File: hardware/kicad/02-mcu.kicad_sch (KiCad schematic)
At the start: 7 parts, among them U1 ESP32-S3-N16R8

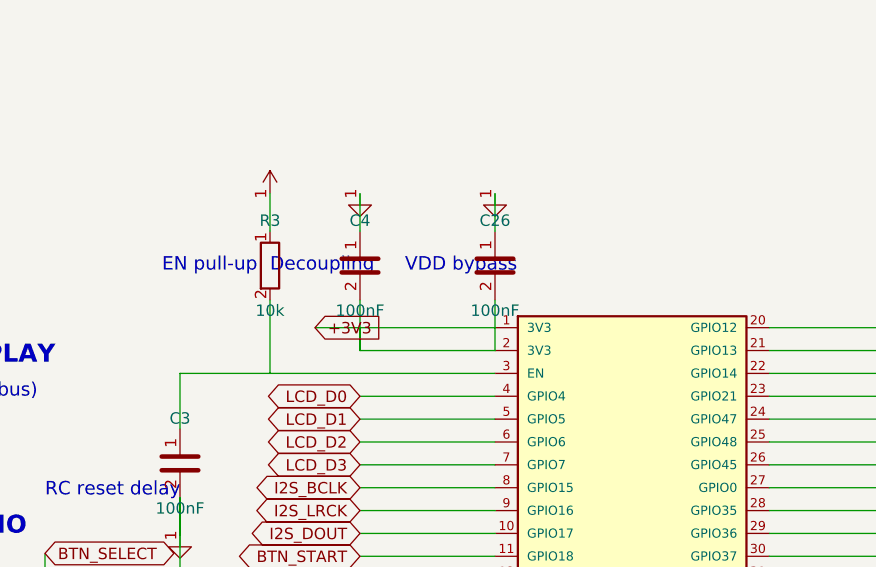
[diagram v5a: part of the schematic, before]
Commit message: fix(hw): R4 audit — schematic↔PCB sync guard + 4 fixes + R4-CRIT-1 false-positive closure
Round 4 of the hardware audit found four real schematic/PCB drift bugs
that rounds 1-3 missed because no check cross-validated the two Python
generators. A fifth finding (R4-CRIT-1, "FPC pinout mismatch") turned
out to be a FALSE POSITIVE caused by the landscape FPC pin reversal
(connector_pad = 41 − panel_pin) — verified programmatically against
all 40 J4 pads of the panel datasheet in components.md.

Fixes applied:
  R4-HIGH-1  USBLC6 (U4) + R22/R23 instantiated in power_supply.py —
             previously only in routing.py, invisible to schematic
             review.
  R4-HIGH-2  Display module symbol ref renamed U4 → DS1 in display.py.
             U4 is now cleanly owned by the physical USBLC6 TVS.
  R4-HIGH-3  PAM8403 R20/R21 input bias moved from GND to VREF
             (pin 8) per the datasheet single-ended app circuit.
  R4-CRIT-1  CLOSED as false positive. Both display.py (panel-side)
             and datasheet_specs.py (connector-side) were correct all
             along. Added 41-N reversal documentation at the top of
             both files so the mistake can't be re-raised.
  ERC CRIT   Pre-existing "Power output ↔ Power output" on +5V was
             PWR_FLAG duplicating IP5306 VOUT (already power_out in the
             library symbol). Removed the PWR_FLAG. ERC now 0 critical.

Incidental cleanups required by the new sync guard:
  - mcu.py R3 (external EN pull-up) removed from schematic — already
    DNP in BOM because the WROOM-1 module has an internal pull-up.
  - controls.py D1 BAT54C (MENU combo diode) instantiated in schematic
    to match the PCB routing. MENU button wiring simplified to the
    MENU_K node; there is no dedicated BTN_MENU GPIO (firmware detects
    START+SELECT combo).
  - power_supply.py USB_CC1 / USB_CC2 global labels added so the
    connector-net coverage check sees the full USB-C net set.
  - display.py docstring expanded with the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
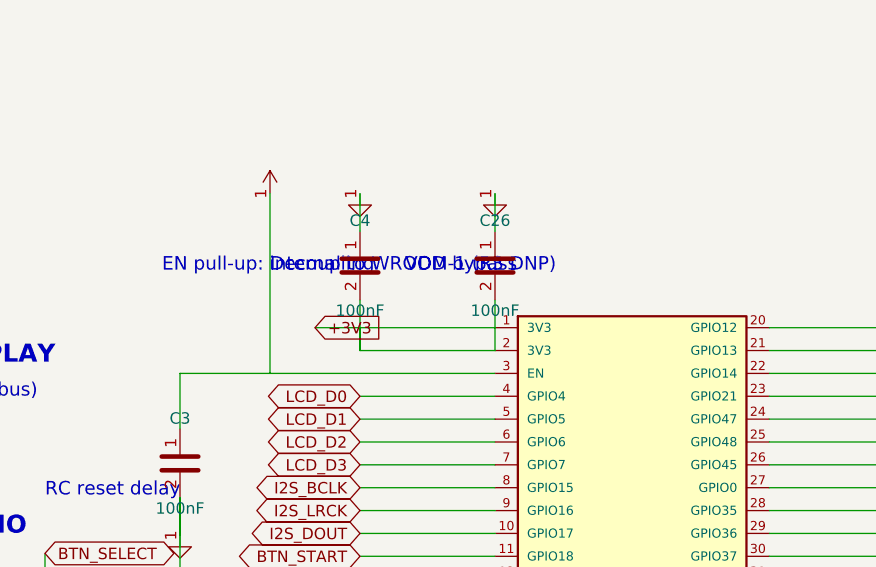
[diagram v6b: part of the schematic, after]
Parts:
- removed R3: 10k, symbol R
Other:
- note added: "EN pull-up: internal to WROOM-1 (R3 DNP)"
- note removed: "EN pull-up"
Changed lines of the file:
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@@
   (wire (pts (xy 184.76 134.44) (xy 169.76 134.44)) (stroke (width 0) (type default)))
   (wire (pts (xy 169.76 134.44) (xy 169.76 131.9)) (stroke (width 0) (type default)))
-  (symbol (lib_id "R") (at 159.76 125 0) (unit 1) (exclude_from_sim no) (in_bom yes) (on_board yes) (dnp no) (property "Reference" "R3" (at 159.76 120 0) (effects (font (size 1.27 1.27)))) (property "Value" "10k" (at 159.76 130 0) (effects (font (size 1.27 1.27)))) (pin "1") (pin "2"))
+  (symbol (lib_id "+3V3") (at 159.76 117 0) (unit 1) (exclude_from_sim no) (in_bom no) (on_board no) (dnp no) (property "Reference" "#PWR001" (at 159.76 115 0) (effects (font (size 1.27 1.27)) hide)) (property "Value" "+3V3" (at 159.76 119 0) (effects (font (size 1.27 1.27)) hide)) (pin "1"))
+  (wire (pts (xy 159.76 117) (xy 159.76 136.98)) (stroke (width 0) (type default)))
   (wire (pts (xy 184.76 136.98) (xy 159.76 136.98)) (stroke (width 0) (type default)))
-  (wire (pts (xy 159.76 136.98) (xy 159.76 128.81)) (stroke (width 0) (type default)))
-  (symbol (lib_id "+3V3") (at 159.76 117 0) (unit 1) (exclude_from_sim no) (in_bom no) (on_board no) (dnp no) (property "Reference" "#PWR001" (at 159.76 115 0) (effects (font (size 1.27 1.27)) hide)) (property "Value" "+3V3" (at 159.76 119 0) (effects (font (size 1.27 1.27)) hide)) (pin "1"))
-  (wire (pts (xy 159.76 117) (xy 159.76 121.19)) (stroke (width 0) (type default)))
-  (text "EN pull-up" (at 147.76 125 0) (effects (font (size 1.5 1.5)) (justify left)))
+  (text "EN pull-up: internal to WROOM-1 (R3 DNP)" (at 147.76 125 0) (effects (font (size 1.5 1.5)) (justify left)))
   (symbol (lib_id "C") (at 149.76 146.98 0) (unit 1) (exclude_from_sim no) (in_bom yes) (on_board yes) (dnp no) (property "Reference" "C3" (at 149.76 141.98 0) (effects (font (size 1.27 1.27)))) (property "Value" "100nF" (at 149.76 151.98 0) (effects (font (size 1.27 1.27)))) (pin "1") (pin "2"))
   (wire (pts (xy 159.76 136.98) (xy 149.76 136.98)) (stroke (width 0) (type default)))

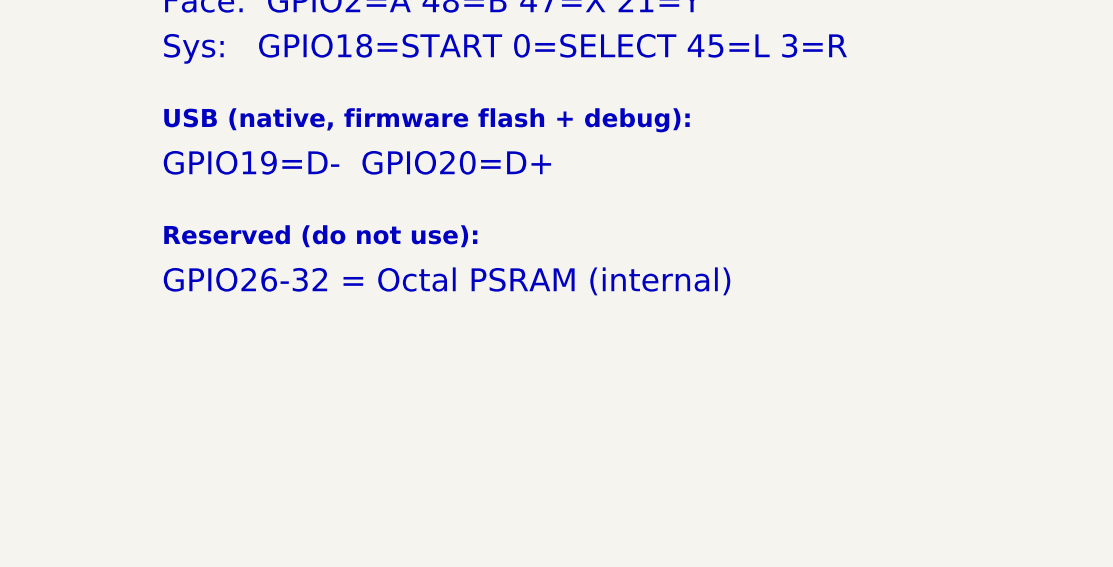
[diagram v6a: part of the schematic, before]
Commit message: docs(R10): close 8 LOW-severity doc-drift findings from Layer 2 audit
Round 10 hardware-audit Layer 2 prose pass found no functional bugs
(0 CRIT/HIGH/MED) but surfaced 8 stale comments and doc-drift items
across schematic generator text labels, datasheet_specs.py function
strings, verify_strapping_pins.py RC timing math, and
snes-optimization.md. All fixed in this single commit — no PCB
regeneration, no routing/geometry changes.

- R10-LOW-1: mcu.py GPIO table labeled "GPIO26-32 = Octal PSRAM" but
  those are actually Octal Flash pins on ESP32-S3-WROOM-1 N16R8.
  PSRAM is on GPIO33-37. Relabeled to show both Flash and PSRAM.

- R10-LOW-2: audio.py I2S bus reference text said "BCLK 1.411MHz @
  44.1kHz" but firmware uses PDM TX (no BCLK/LRCK) at 32kHz.
  Relabeled GPIO15/16 as UNUSED with a v2-reuse note (candidates for
  ADC2 battery voltage). Dead-net removal deferred to v2 respin.

- R10-LOW-3: sd_card.py said "SPI @ up to 40MHz" but firmware runs
  20MHz (R2-MED-5 trace-length cap). Updated design-note text.

- R10-LOW-4: sd_card.py said "GPIO36-39 grouped for clean SPI" but
  actual SPI pins are GPIO38/39 (CLK/CS) + GPIO43/44 (MISO/MOSI) —
  split across the WROOM-1 module. Updated design-note text.

- R10-LOW-5: datasheet_specs.py J4 pads 15/16 function strings said
  "NC (IM0/IM1 mode select)" but after the 41-N panel pin reversal
  those pads correspond to DB9/DB8 (unused upper data bits in 8-bit
  8080 mode). IM0/IM1 are actually on J4 pads 3/2. Fixed function
  strings with a comment explaining the 41-N mapping.

- R10-LOW-6: datasheet_specs.py U5 block comment said "left channel
  only: OUTL+ → SPK+, OUTL- → SPK-" but the pad map wires SPK± to
  OUTR+/OUTR- (pins 14/16). OUTL+/- are floating. Rewrote the
  comment + pin 1/3 function strings to match the actual wiring.

- R10-LOW-7: verify_strapping_pins.py test_en_rc_delay() computed
  tau = 10kΩ·100nF = 1ms assuming external R3, but R4 closed R3 as
  DNP and the WROOM-1 module integrates a ~45kΩ EN pull-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
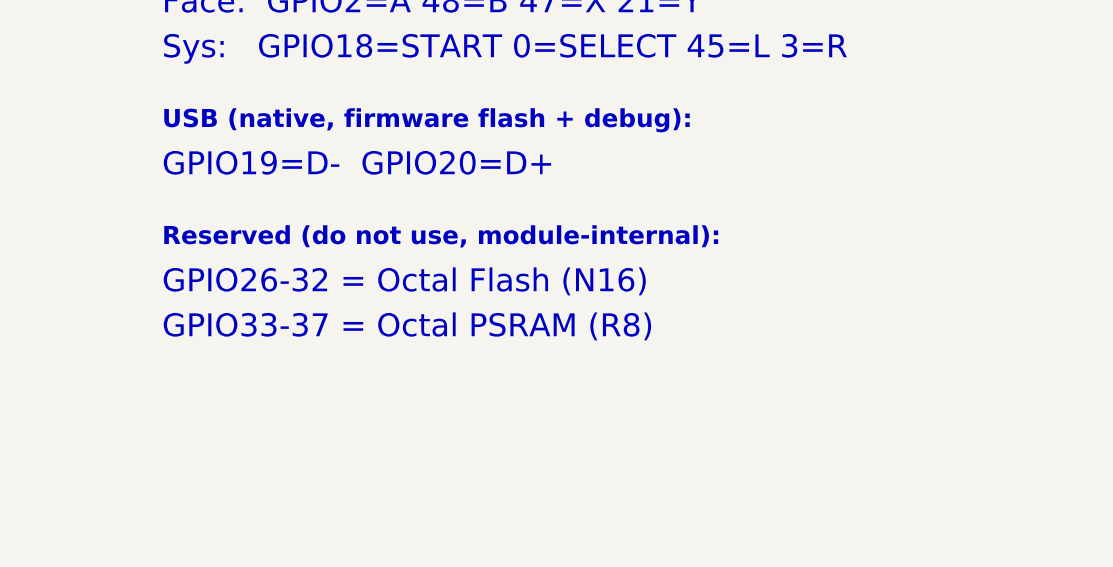
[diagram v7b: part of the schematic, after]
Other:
- note added: "GPIO26-32 = Octal Flash (N16)"
- note added: "GPIO33-37 = Octal PSRAM (R8)"
- note added: "Reserved (do not use, module-internal):"
- note removed: "GPIO26-32 = Octal PSRAM (internal)"
- note removed: "Reserved (do not use):"
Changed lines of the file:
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@@
   (text "USB (native, firmware flash + debug):" (at 320 112 0) (effects (font (size 2 2) bold) (justify left)))
   (text "GPIO19=D-  GPIO20=D+" (at 320 117 0) (effects (font (size 2.54 2.54)) (justify left)))
-  (text "Reserved (do not use):" (at 320 125 0) (effects (font (size 2 2) bold) (justify left)))
-  (text "GPIO26-32 = Octal PSRAM (internal)" (at 320 130 0) (effects (font (size 2.54 2.54)) (justify left)))
+  (text "Reserved (do not use, module-internal):" (at 320 125 0) (effects (font (size 2 2) bold) (justify left)))
+  (text "GPIO26-32 = Octal Flash (N16)" (at 320 130 0) (effects (font (size 2.54 2.54)) (justify left)))
+  (text "GPIO33-37 = Octal PSRAM (R8)" (at 320 135 0) (effects (font (size 2.54 2.54)) (justify left)))
   (sheet_instances (path "/" (page "2")))
 )
